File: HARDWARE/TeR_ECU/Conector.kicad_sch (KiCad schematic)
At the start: 1 part, among them IC1 MX34040NF2

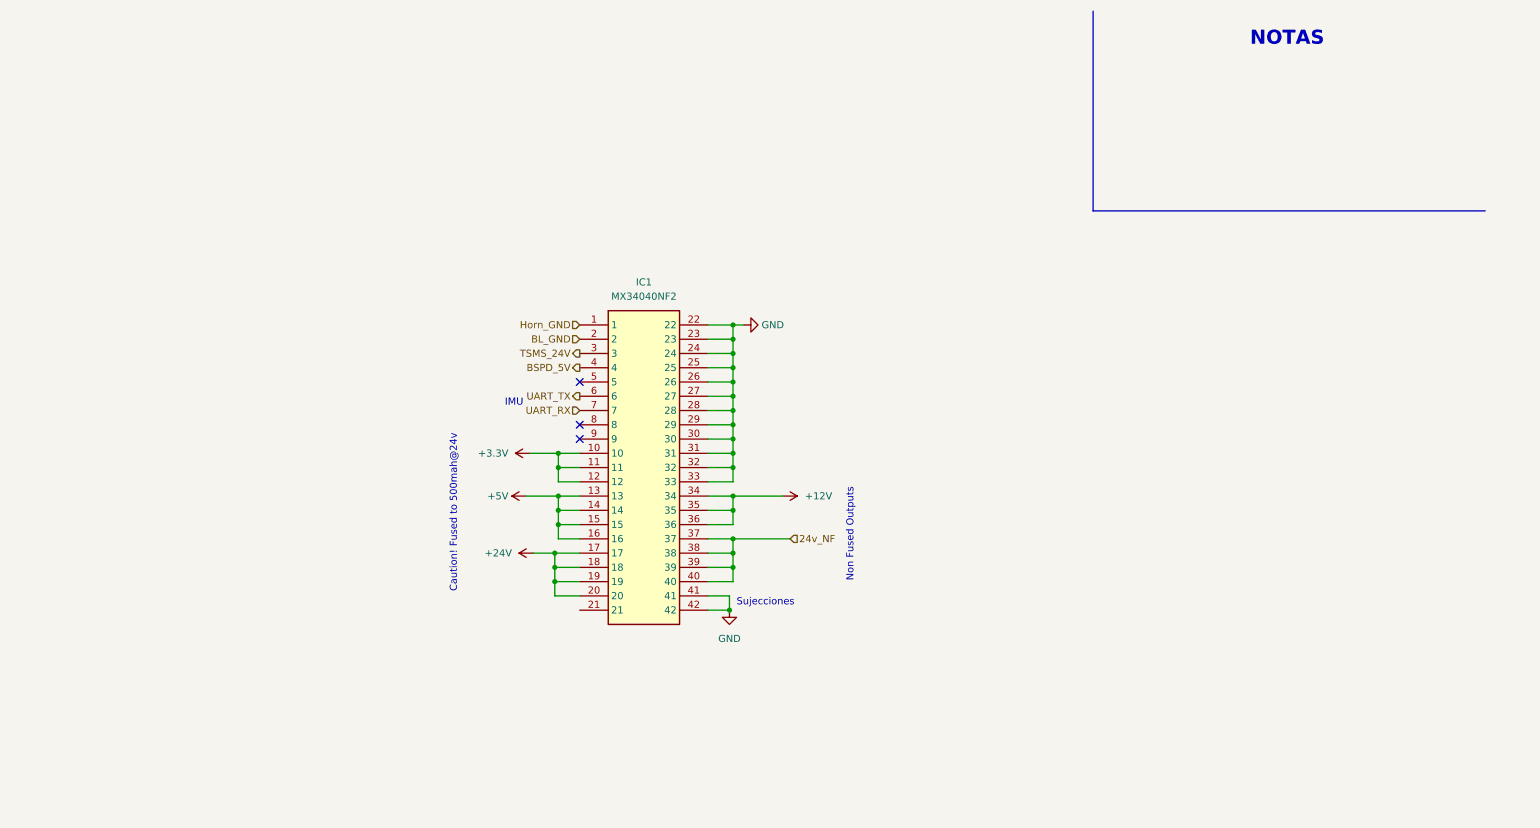
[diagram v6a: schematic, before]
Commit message: idea de esquema de safety y level shifter para señales de 24v
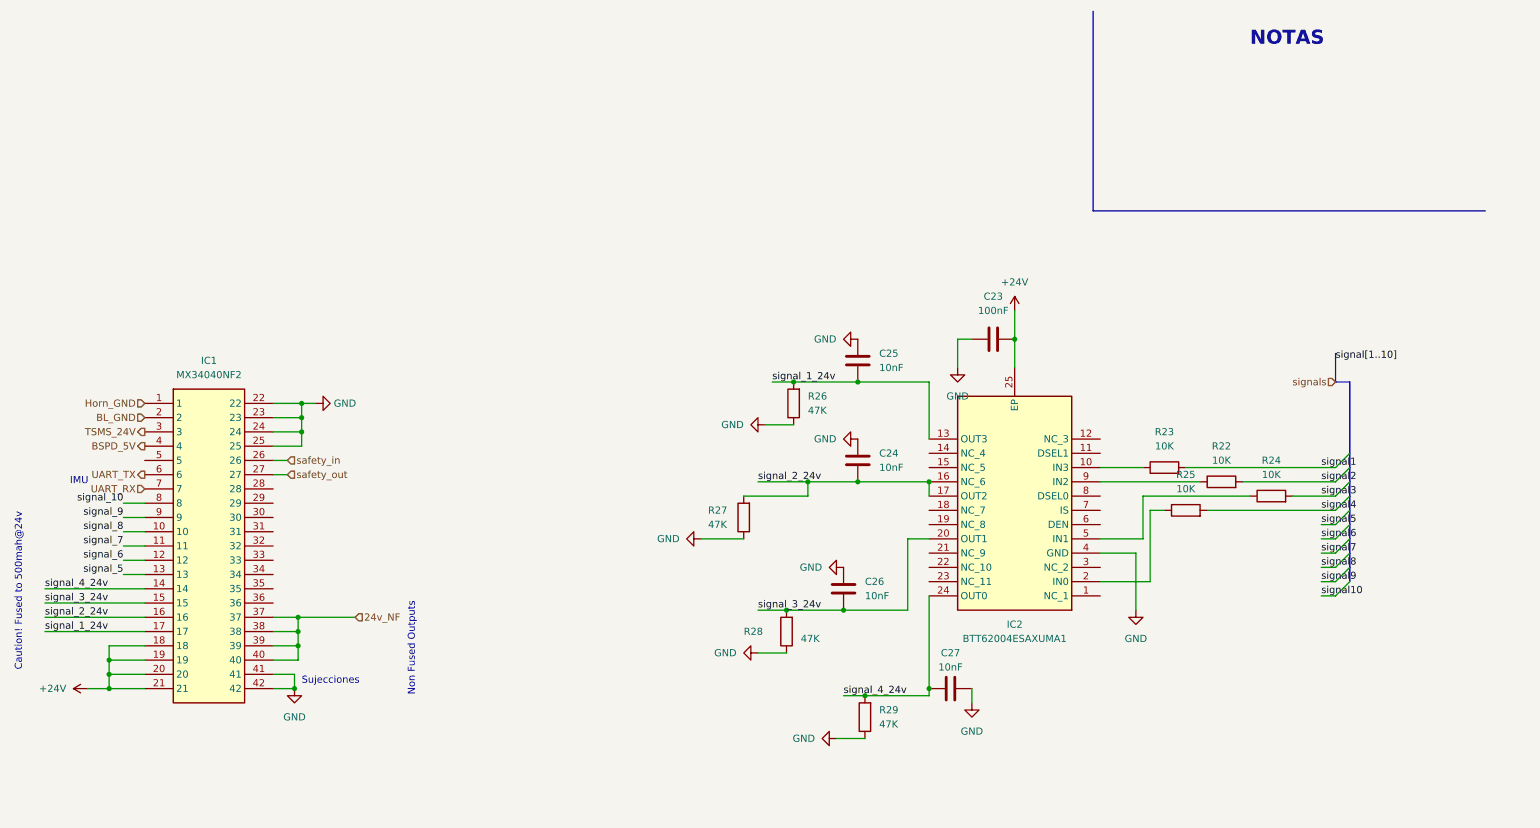
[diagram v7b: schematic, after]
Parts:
- added C23: 100nF, symbol Device:C
- added C24, C25, C26, C27: 10nF, symbol Device:C
- added IC2: BTT62004ESAXUMA1, SOP65P600X115-25N, symbol BTT62004ESAXUMA1:BTT62004ESAXUMA1
- added R22, R23, R24, R25: 10K, symbol Device:R
- added R26, R27, R28, R29: 47K, symbol Device:R
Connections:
- net +24V: now also IC1.21, C23.2, IC2.25 (EP); no longer IC1.17
- net GND: now also C23.1, C24.1, C25.1, C26.1, C27.1, IC2.4 (GND), R26.1, R27.1, R28.1, R29.1; no longer IC1.26, IC1.27, IC1.28, IC1.29, IC1.30, IC1.31, IC1.32, IC1.33
- net signal_10: now reaches IC1.8
- net signal_9: now reaches IC1.9
- removed net +12V: IC1.34, IC1.35, IC1.36
- removed net +3.3V: IC1.10, IC1.11, IC1.12
- removed net +5V: IC1.13, IC1.14, IC1.15, IC1.16
- new net: IC2.10 (IN3), R23.1
- new net: IC2.2 (IN0), R25.1
- new net: IC2.5 (IN1), R24.1
- new net: IC2.9 (IN2), R22.1
- new net safety_in: IC1.26
- new net safety_out: IC1.27
- new net signal1: R23.2
- new net signal2: R22.2
- new net signal3: R24.2
- new net signal4: R25.2
- new net signal_1_24v: C25.2, IC1.17, IC2.13 (OUT3), R26.2
- new net signal_2_24v: C24.2, IC1.16, IC2.16 (NC_6), IC2.17 (OUT2), R27.2
- new net signal_3_24v: C26.2, IC1.15, IC2.20 (OUT1), R28.2
- new net signal_4_24v: C27.2, IC1.14, IC2.24 (OUT0), R29.2
- new net signal_5: IC1.13
- new net signal_6: IC1.12
- new net signal_7: IC1.11
- new net signal_8: IC1.10
- no-connect marks 3 -> 0
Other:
- moved on the sheet: IC1

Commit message: ic comments
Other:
- note added: "esta es la idea, conseguir shiftear la señal 3.3 a 24v de momento usaremos este ic, pero lo que realmente importa es la idea"
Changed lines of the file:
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@@
     (stroke (width 0) (type default))
+  )
+  (rectangle (start 129.54 53.34) (end 274.32 156.21)
+    (stroke (width 0) (type dot))
+    (fill (type none))
   )
   (text "IMU" (at 33.655 97.155 0)
@@
     (effects (font (size 2.5 2.5) (thickness 0.5) bold) (justify left bottom))
   )
+  (text "esta es la idea, conseguir shiftear la señal 3.3 a 24v\nde momento usaremos este ic, pero lo que\nrealmente importa es la idea"
+    (at 135.89 50.8 0)
+    (effects (font (size 1.27 1.27)) (justify left bottom))
+  )
   (label "signal_3_24v" (at 156.21 119.38 0) (fields_autoplaced)
